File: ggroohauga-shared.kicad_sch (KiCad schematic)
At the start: 13 parts

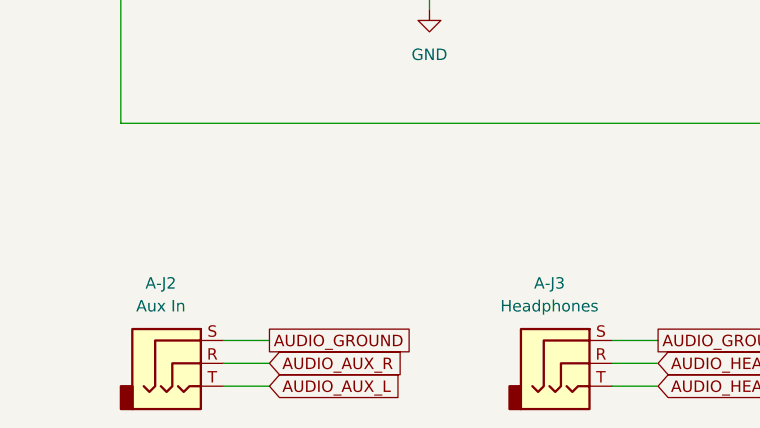
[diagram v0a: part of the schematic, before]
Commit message: Fix component references for audio jacks
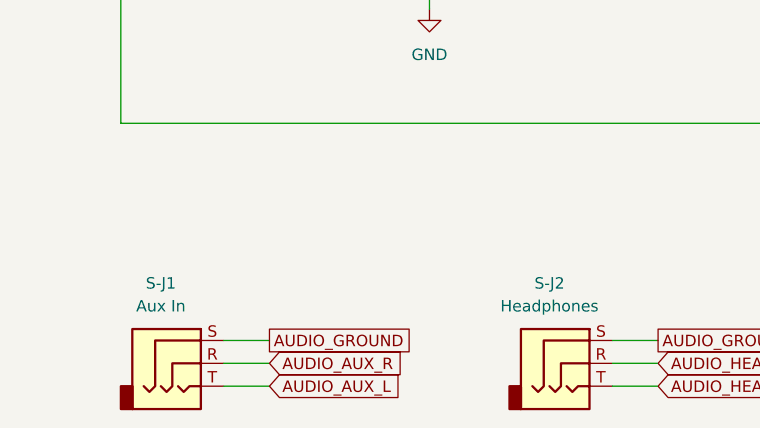
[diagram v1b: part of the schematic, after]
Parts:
- renumbered A-J2 to S-J1, A-J3 to S-J2
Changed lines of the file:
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@@
 		(dnp no)
 		(fields_autoplaced yes)
-		(property "Reference" "A-J2"
+		(property "Reference" "S-J1"
 			(at 33.655 172.72 0)
 			(effects
@@
 			(project "ggroohauga-amplifier"
 				(path "/40d11306-2494-4bd8-b540-c25b2be9aaac/d8f68aac-e4b3-42cf-adb2-95c1a8c35ecf"
-					(reference "A-J2")
+					(reference "S-J1")
 					(unit 1)
 				)
@@
 		(dnp no)
 		(fields_autoplaced yes)
-		(property "Reference" "A-J3"
+		(property "Reference" "S-J2"
 			(at 76.835 172.72 0)
 			(effects
@@
 			(project "ggroohauga-amplifier"
 				(path "/40d11306-2494-4bd8-b540-c25b2be9aaac/d8f68aac-e4b3-42cf-adb2-95c1a8c35ecf"
-					(reference "A-J3")
+					(reference "S-J2")
 					(unit 1)
 				)

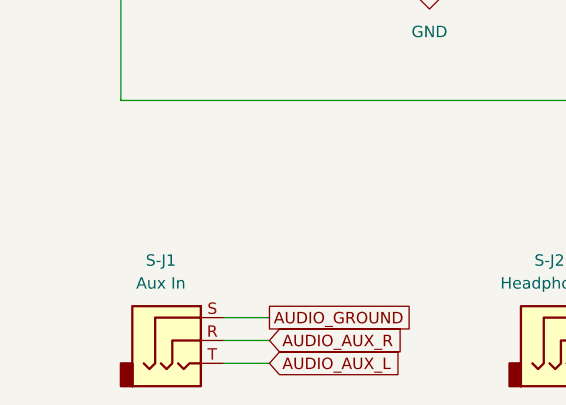
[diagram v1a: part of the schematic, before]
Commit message: Rename "Aux In" to "Aux Input" and document 3.5mm audio sockets
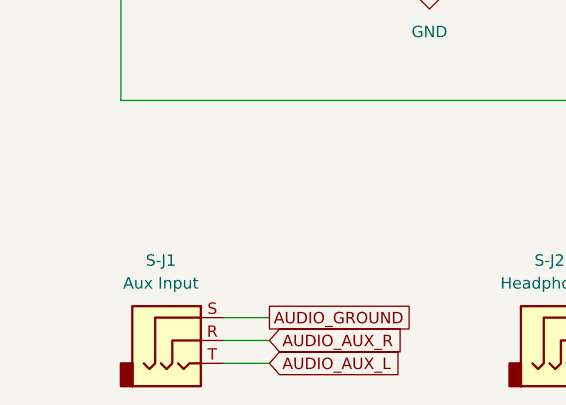
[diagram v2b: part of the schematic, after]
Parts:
- S-J1: value Aux In -> Aux Input
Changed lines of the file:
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@@
 			)
 		)
-		(property "Value" "Aux In"
+		(property "Value" "Aux Input"
 			(at 33.655 175.26 0)
 			(effects

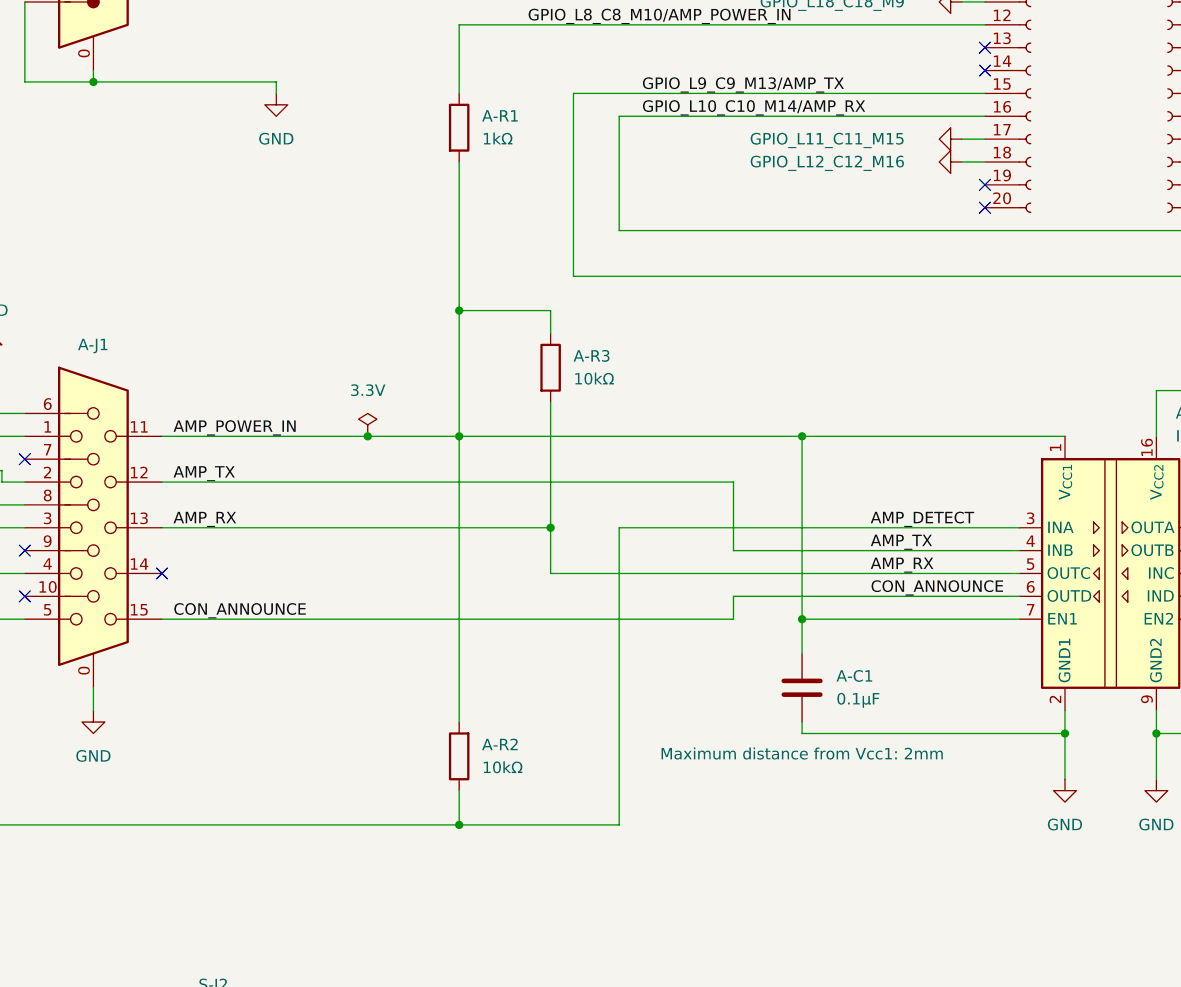
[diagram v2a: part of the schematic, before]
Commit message: Move pull-up from AMP_RX to AMP_TX
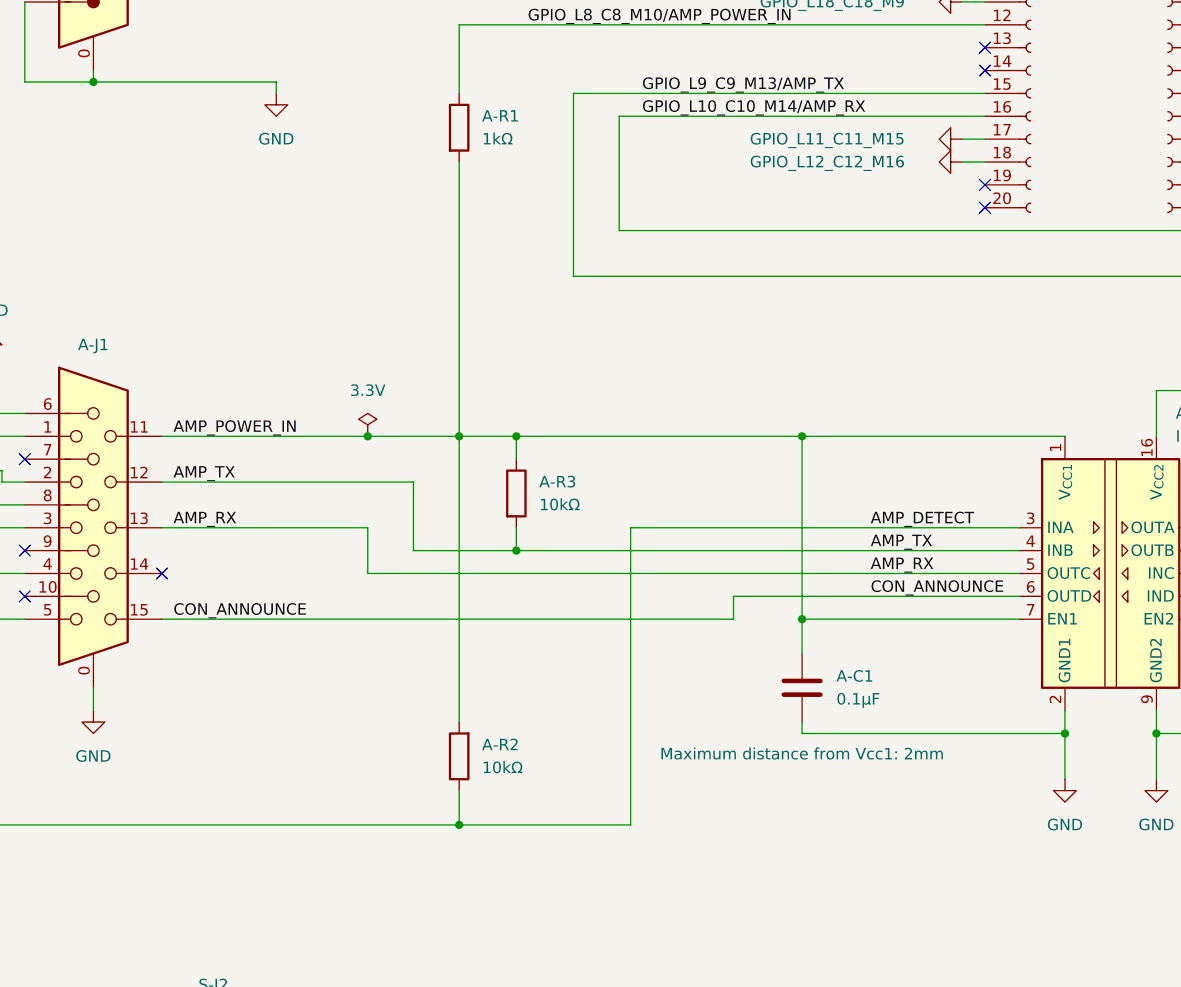
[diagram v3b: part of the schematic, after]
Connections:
- net AMP_RX: no longer A-R3.2
- net AMP_TX: now also A-R3.2
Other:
- moved on the sheet: A-R3
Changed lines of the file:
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@@
+	)
+	(junction
+		(at 110.49 124.46)
+		(diameter 0)
+		(color 0 0 0 0)
 	)
 	(junction
@@
 	)
 	(junction
-		(at 114.3 121.92)
-		(diameter 0)
-		(color 0 0 0 0)
-	)
-	(junction
 		(at 104.14 154.94)
 		(diameter 0)
@@
 	)
 	(junction
+		(at 110.49 111.76)
+		(diameter 0)
+		(color 0 0 0 0)
+	)
+	(junction
 		(at 171.45 144.78)
 		(diameter 0)
 		(color 0 0 0 0)
 	)
-	(junction
-		(at 104.14 97.79)
-		(diameter 0)
-		(color 0 0 0 0)
-	)
 	(no_connect
 		(at 55.88 58.42)
@@
 	(wire
 		(pts
-			(xy 71.12 116.84) (xy 134.62 116.84)
+			(xy 71.12 116.84) (xy 99.06 116.84)
 		)
 		(stroke
@@
 	(wire
 		(pts
+			(xy 110.49 111.76) (xy 142.24 111.76)
+		)
+		(stroke
+			(width 0)
+			(type default)
+		)
+	)
+	(wire
+		(pts
 			(xy 256.54 22.86) (xy 104.14 22.86)
 		)
@@
 	(wire
 		(pts
-			(xy 104.14 111.76) (xy 142.24 111.76)
+			(xy 104.14 111.76) (xy 110.49 111.76)
 		)
 		(stroke
@@
 	(wire
 		(pts
-			(xy 121.92 121.92) (xy 166.37 121.92)
+			(xy 123.19 121.92) (xy 166.37 121.92)
 		)
 		(stroke
@@
 	(wire
 		(pts
-			(xy 134.62 116.84) (xy 134.62 124.46)
+			(xy 99.06 116.84) (xy 99.06 124.46)
 		)
 		(stroke
@@
 	(wire
 		(pts
-			(xy 104.14 154.94) (xy 121.92 154.94)
+			(xy 104.14 154.94) (xy 123.19 154.94)
 		)
 		(stroke
@@
 	(wire
 		(pts
-			(xy 104.14 81.28) (xy 104.14 97.79)
+			(xy 104.14 81.28) (xy 104.14 111.76)
 		)
 		(stroke
@@
 	(wire
 		(pts
-			(xy 134.62 124.46) (xy 166.37 124.46)
+			(xy 99.06 124.46) (xy 110.49 124.46)
 		)
 		(stroke
@@
 	(wire
 		(pts
-			(xy 114.3 127) (xy 114.3 121.92)
+			(xy 93.98 127) (xy 93.98 121.92)
 		)
 		(stroke
@@
 	(wire
 		(pts
+			(xy 110.49 111.76) (xy 110.49 114.3)
+		)
+		(stroke
+			(width 0)
+			(type default)
+		)
+	)
+	(wire
+		(pts
 			(xy 256.54 144.78) (xy 256.54 143.51)
 		)
@@
 	(wire
 		(pts
-			(xy 71.12 121.92) (xy 114.3 121.92)
+			(xy 71.12 121.92) (xy 93.98 121.92)
 		)
 		(stroke
@@
 	(wire
 		(pts
-			(xy 104.14 97.79) (xy 114.3 97.79)
-		)
-		(stroke
-			(width 0)
-			(type default)
-		)
-	)
-	(wire
-		(pts
 			(xy 171.45 142.24) (xy 171.45 144.78)
 		)
@@
 	(wire
 		(pts
-			(xy 104.14 97.79) (xy 104.14 111.76)
-		)
-		(stroke
-			(width 0)
-			(type default)
-		)
-	)
-	(wire
-		(pts
 			(xy 245.11 68.58) (xy 245.11 129.54)
 		)
@@
 	(wire
 		(pts
-			(xy 114.3 127) (xy 166.37 127)
+			(xy 93.98 127) (xy 166.37 127)
 		)
 		(stroke
@@
 	(wire
 		(pts
-			(xy 114.3 97.79) (xy 114.3 100.33)
-		)
-		(stroke
-			(width 0)
-			(type default)
-		)
-	)
-	(wire
-		(pts
 			(xy 50.8 55.88) (xy 55.88 55.88)
 		)
@@
 	(wire
 		(pts
-			(xy 114.3 107.95) (xy 114.3 121.92)
-		)
-		(stroke
-			(width 0)
-			(type default)
-		)
-	)
-	(wire
-		(pts
-			(xy 121.92 121.92) (xy 121.92 154.94)
+			(xy 123.19 121.92) (xy 123.19 154.94)
 		)
 		(stroke
@@
 	(wire
 		(pts
+			(xy 110.49 121.92) (xy 110.49 124.46)
+		)
+		(stroke
+			(width 0)
+			(type default)
+		)
+	)
+	(wire
+		(pts
 			(xy 116.84 73.66) (xy 116.84 93.98)
 		)
@@
 		(pts
 			(xy 142.24 132.08) (xy 166.37 132.08)
+		)
+		(stroke
+			(width 0)
+			(type default)
+		)
+	)
+	(wire
+		(pts
+			(xy 110.49 124.46) (xy 166.37 124.46)
 		)
 		(stroke
@@
 	(symbol
 		(lib_id "Device:R")
-		(at 114.3 104.14 0)
+		(at 110.49 118.11 0)
 		(unit 1)
 		(exclude_from_sim no)
@@
 		(fields_autoplaced yes)
 		(property "Reference" "A-R3"
-			(at 116.84 102.8699 0)
+			(at 113.03 116.8399 0)
 			(effects
 				(font
@@
 		)
 		(property "Value" "10kΩ"
-			(at 116.84 105.4099 0)
+			(at 113.03 119.3799 0)
 			(effects
 				(font
@@
 		)
 		(property "Footprint" "Resistor_SMD:R_0805_2012Metric_Pad1.20x1.40mm_HandSolder"
-			(at 112.522 104.14 90)
+			(at 108.712 118.11 90)
 			(effects
 				(font
@@
 		)
 		(property "Datasheet" "~"
-			(at 114.3 104.14 0)
+			(at 110.49 118.11 0)
 			(effects
 				(font
@@
 		)
 		(property "Description" "Resistor"
-			(at 114.3 104.14 0)
-			(effects
-				(font
+			(at 110.49 118.11 0)
+			(effects
+				(font

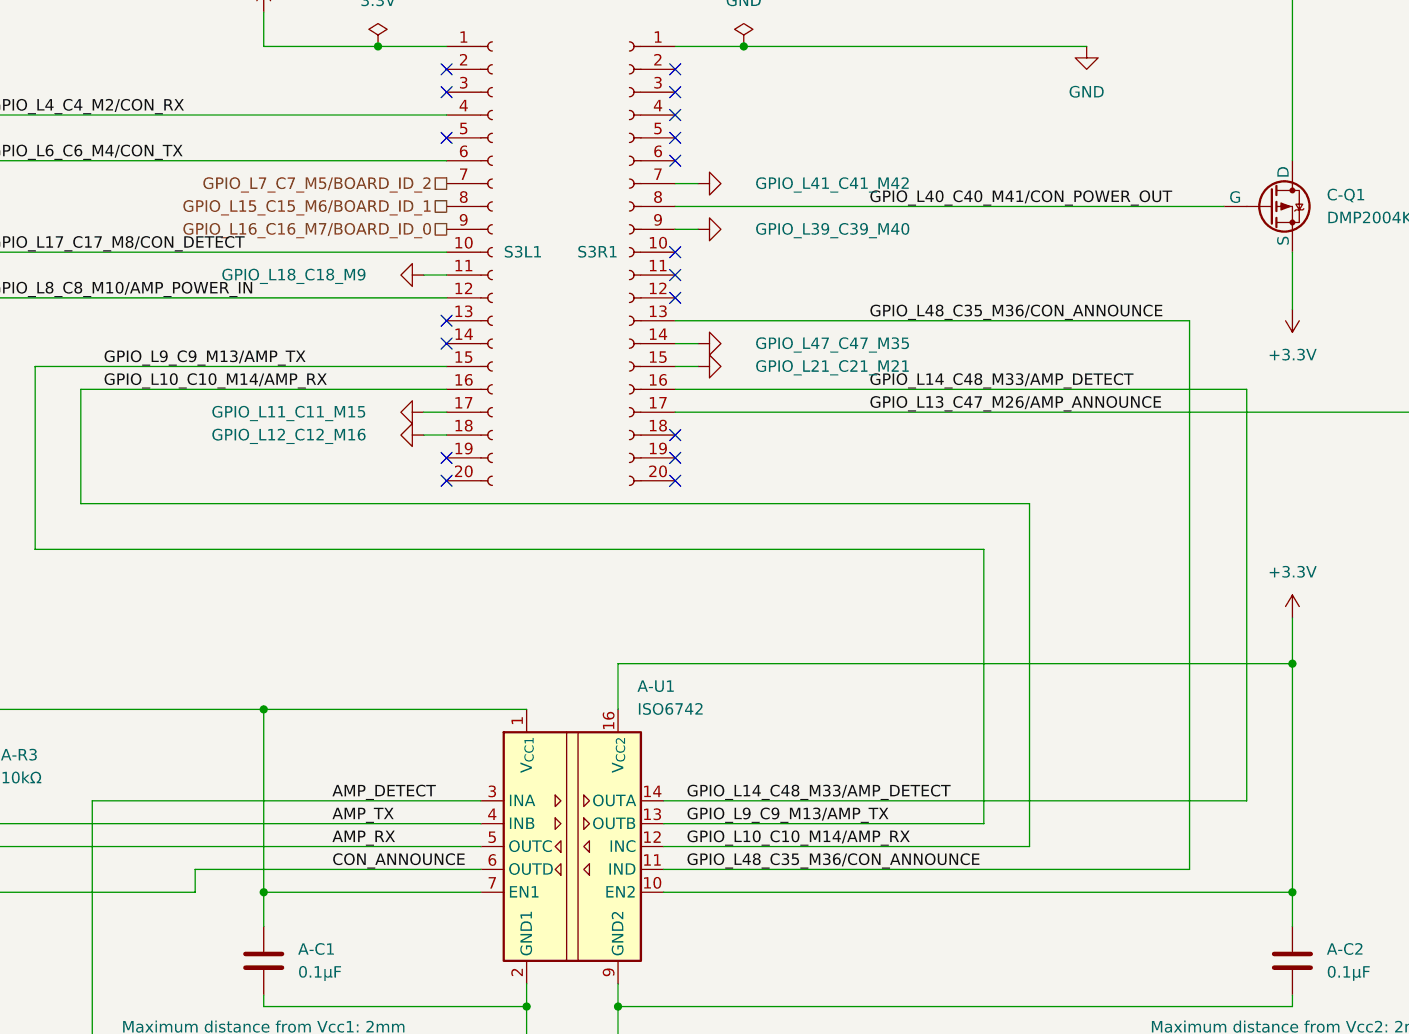
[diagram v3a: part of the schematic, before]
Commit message: Fix GPIO assignments
Stop using GPIO 14 because the pull-up isn't working reliably on my LOLIN
S3 board even when floating and I don't have another one to test it with.

Don't use GPIO 35 on the DevKitC-1 board because that conflicts with the
Octal PSRAM.
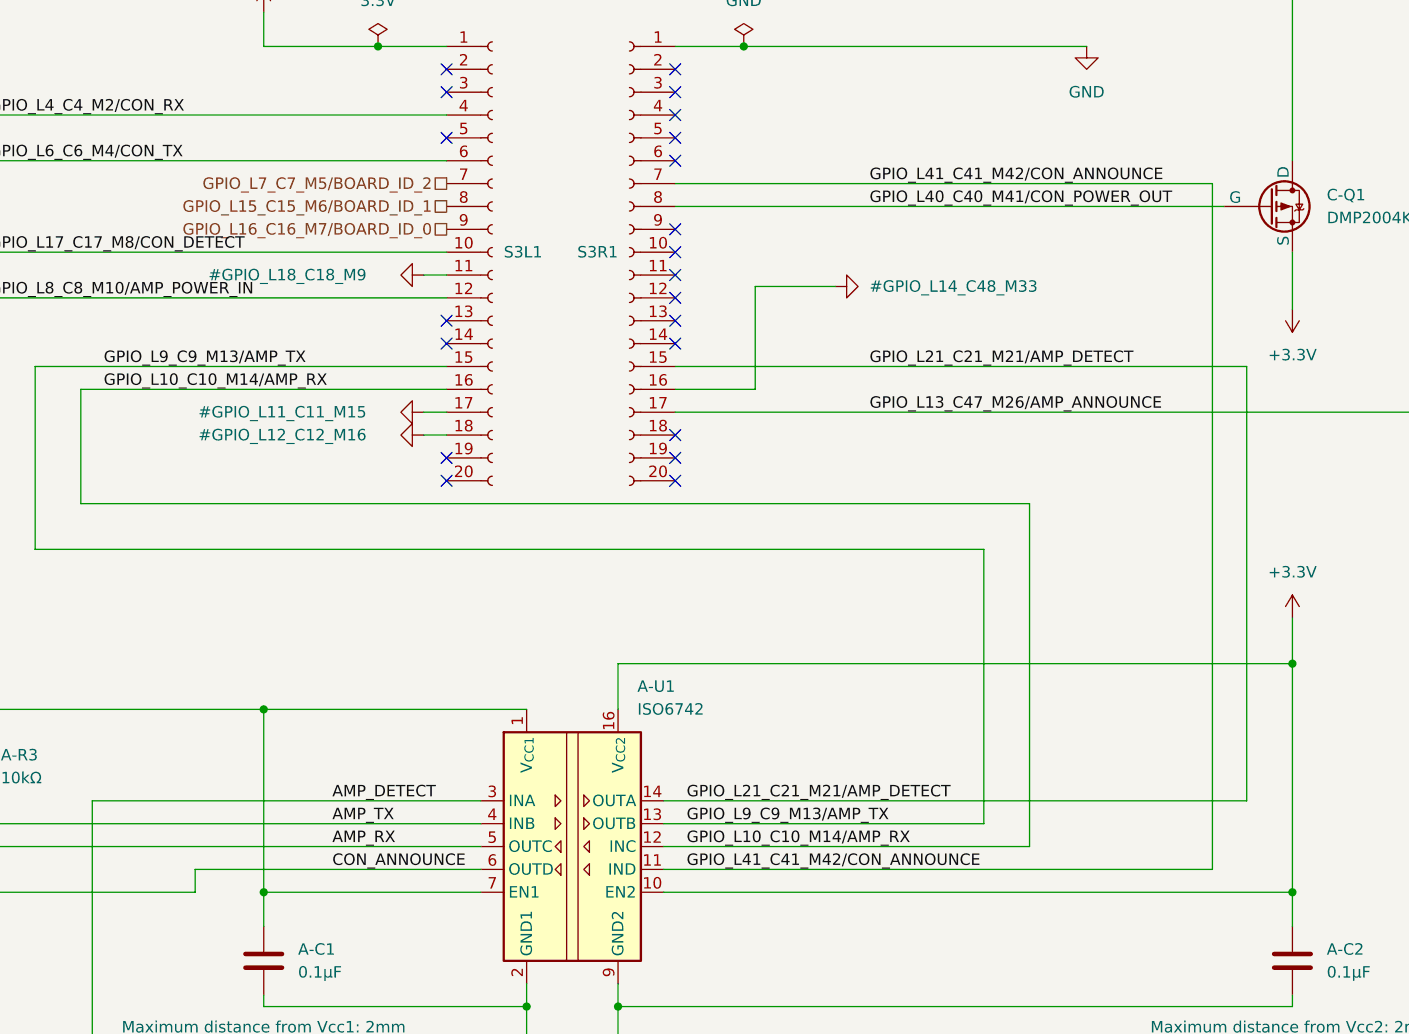
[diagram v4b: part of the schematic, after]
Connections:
- net GND: now also S3R1.16 (Pin_16); no longer S3R1.14 (Pin_14), S3R1.15 (Pin_15), S3R1.7 (Pin_7), S3R1.9 (Pin_9)
- net GPIO_L14_C48_M33/AMP_DETECT renamed GPIO_L21_C21_M21/AMP_DETECT
- net GPIO_L21_C21_M21/AMP_DETECT: now also S3R1.15 (Pin_15); no longer S3R1.16 (Pin_16)
- net GPIO_L48_C35_M36/CON_ANNOUNCE: no longer names the net of S3R1.13 (Pin_13)
- net GPIO_L48_C35_M36/CON_ANNOUNCE: no longer A-U1.11 (IND)
- new net GPIO_L41_C41_M42/CON_ANNOUNCE: A-U1.11 (IND), S3R1.7 (Pin_7)
- no-connect marks 26 -> 29
